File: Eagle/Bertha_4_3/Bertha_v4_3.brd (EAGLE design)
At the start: 100 x 84.6 mm, 89 parts, among them CON1 JACK_DC_BARREL, IC1 MCP1703DB, J1 RJ12RIGHTANGLE-I2C, J2 RJ12RIGHTANGLE-I2C, Q5 BSP75, Q6 BSP75, U1 HX711, X2 16MHz, X3 FH12-08S-1SH, X4 MINI-USB

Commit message: new v4.3, removed bistable control of the stepper, now on pins A0/A1/D8/D9, control sequence must be adapted in the arduino code. Started to work on the ph_V5.0 board, need to add two steppers and the analog backend circuit
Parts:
- removed 5V1: (no value), Headerlibrary:1X01
- removed C16, C17: 100nF, rcl:C1206
- removed CU5, CU6: 10uF, rcl:C1206
- removed D3, D5: 1N581D1206, lpatiny:LED-1206
- removed LDPW5: RED, adafruit:CHIP-LED0805
- removed R13: 1k, resistor:R0805
- removed R8: 1K, rcl:R0805
- removed U$2: NCP1117LPST50T3G, lpatiny:SOT223
- removed U$6: TXB0104, lpatiny:SO14
- added 100K: 100k, rcl:R0805
- added AN_OUT, LORA_RST: (no value), Headerlibrary:1X01
- added C3, C4: 100nF, rcl:C1206
- added HX1: IRF3704S, transistor-power:D2PACK
- added J7: 22--02, lpatiny:2-PIN-5.08S
- added JP2: (no value), SparkFun-Connectors:1X02
- added LDM1, LDM2, LDM3, LDM4, LDPID, RXLD, TXLD: RED, adafruit:CHIP-LED0805
- added Q1, Q2, Q3, Q4: BSP75, infineon:PG-SOT-223
- added R10, R11, R9: 1K, rcl:R0805
- added RK10, RK11, RK8, RK9: 10K, rcl:R0805
- added RK14, RK15, RK16: 10k, rcl:R0805
- added RT1, RT2: 4.7k, resistor:R1206
- added SJ4, SJ5, SJ6: (no value), SparkFun-Passives:PAD-JUMPER-2-NC_BY_TRACE_YES_SILK
- added STEPPER: (no value), con-lsta:FE06
- added U$4: DS18B20, lpatiny:SO8
- added U$8: DS18B20_SMALLPADS, lpatiny:SMALLPADS_X3
- added U100: RN2483, Octanis1:RN2483
- X2: value 16MHz -> 8MHz
- moved C2 19.0 mm to (35.8, 19.1)
- moved CU4 18.9 mm to (35.8, 16.3)
- moved R12 16.0 mm to (10.7, 23.3), turned to 180 degrees
- moved LDPW12 9.76 mm to (15.2, 23.3), turned to 270 degrees
- moved RK19 7.58 mm to (19.3, 39.3)
- moved LDMEM 6.66 mm to (23.3, 39.3), turned to 270 degrees
- moved LDPW3 4.34 mm to (15.2, 25.8)
- moved R14 4.25 mm to (10.6, 25.8)
- moved IN 1.60 mm to (63.7, 38.8)
- moved CU8 0.59 mm to (5.89, 2.12)
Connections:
- removed net +5V: CU5.1, D3.A, U$2.2, U$2.4
- removed net +5V/1: 32U4.14, 32U4.2, 32U4.24, 32U4.34, 32U4.44, 5V1.1, BJ1.2, C1.1, C12.2, C17.2, C2.1, C6.1, CU1.1, CU3.1, CU4.1, CU7.1, D2.C, D3.C, D4.C, IC1.1, J1.+5V, J2.+5V, R13.1, R8.2, RK1.1, RK18.1, RK19.1, RK2.1, RK5.2, RK6.2, U$6.14, U1.1, U1.16, X3.1, X3.2
- removed net FMOSI: D5.A, RK4.1, U$1.SI
- removed net MISO3: U$1.SO, U$6.4
- removed net MOSI3: D5.C, U$6.3
- removed net N$12: LDPW5.A, R13.2
- removed net N$4: R8.1, U$6.8
- removed net SCK3: RK3.1, U$6.5
- removed net SC_MEM: R3.2, U$6.6
- new net 5: J1.+5V, J2.+5V
- new net ANGND: C3.2, C4.2, SJ4.2, SJ5.2, SJ6.2, U100.P$1, U100.P$11, U100.P$20, U100.P$21, U100.P$22, U100.P$24, U100.P$26, U100.P$27, U100.P$28, U100.P$33, U100.P$41, U100.P$47, U100.P$8
- new net ANT868: AN_OUT.1, U100.P$23
- new net B+: JP2.1, U1.10
- new net B-: JP2.2, U1.9
- new net N$14: Q4.2, RK8.1, STEPPER.1
- new net N$15: Q2.2, RK9.1, STEPPER.3
- new net N$16: Q3.2, RK10.1, STEPPER.4
- new net N$18: RK15.2, TXLD.A
- new net N$19: Q1.2, RK11.1, STEPPER.6
- new net N$21: R9.2, RT1.2, U$8.PIN2
- new net N$24: RK16.2, RXLD.A
- new net N$26: LDPID.A, RK14.1
- new net N$31: LDM4.C, RK8.2
- new net N$32: LDM3.C, RK9.2
- new net N$33: LDM2.C, RK10.2
- new net N$36: HX1.2, J7.2
- new net N$37: LDM1.C, RK11.2
- new net N$6: HX1.1, R11.2, RK14.2
- new net N$9: R10.2, RT2.2, U$4.4
- net +12V: now also C1.1, C2.1, CU3.1, CU4.1, CU7.1, D2.C, D4.C, IC1.1, J7.1, LDM1.A, LDM2.A, LDM3.A, LDM4.A, STEPPER.2, STEPPER.5, X3.1, X3.2; no longer CU6.1, U$2.3
- net 3.3V: now also 100K.1, 32U4.14, 32U4.2, 32U4.24, 32U4.34, 32U4.44, BJ1.2, C12.2, C3.1, C4.1, C6.1, CU1.1, RK1.1, RK15.1, RK16.1, RK18.1, RK19.1, RK2.1, RK5.2, RK6.2, RT1.1, RT2.1, U$4.3, U$8.PIN3, U1.1, U1.16, U100.P$12, U100.P$34; no longer C16.2, U$6.1
- net A0: now also Q3.1
- net A1: now also Q1.1
- net A6: now also R9.1
- net D10*: now also R3.2; no longer U$6.9
- net D12*: now also R11.1
- net D5*: now also 100K.2, LORA_RST.1, U100.P$32
- net D6*: now also R10.1
- net D8*: now also Q4.1
- net D9*: now also Q2.1
- net GND: now also HX1.3, LDPID.C, Q1.3, Q2.3, Q3.3, Q4.3, SJ4.1, SJ5.1, SJ6.1, U$4.5, U$8.PIN1; no longer C16.1, C17.1, CU5.2, CU6.2, LDPW5.C, U$2.1, U$6.7
- net MISO: now also U$1.SO; no longer U$6.11
- net MOSI: now also RK4.1, U$1.SI; no longer U$6.12
- net RX: now also U100.P$6
- net RXLED: now also RXLD.C
- net SCK: now also RK3.1; no longer U$6.10
- net TX: now also U100.P$7
- net TXLED: now also TXLD.C
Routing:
- net +5V/1: track 451.3 -> 0.00 mm, vias 7 -> 0
- net 3.3V: track 182.3 -> 480.4 mm, vias 4 -> 18
- net +12V: track 133.3 -> 334.4 mm, vias 0 -> 2
- net D5*: track 0.00 -> 164.8 mm, vias 0 -> 3
- net RX: track 0.00 -> 102.2 mm, vias 0 -> 5
- net TX: track 0.00 -> 97.3 mm, vias 0 -> 5
- net D12*: track 0.00 -> 63.0 mm, vias 0 -> 2
- net D10*: track 0.00 -> 57.9 mm, vias 0 -> 2
- net A1: track 0.00 -> 48.2 mm, vias 0 -> 2
- net GND: track 124.0 -> 171.7 mm, vias 29 -> 39
- net D8*: track 0.00 -> 39.2 mm, vias 0 -> 2
- net N$14: track 0.00 -> 36.3 mm
- net D9*: track 0.00 -> 35.1 mm, vias 0 -> 2
- net MISO: track 76.9 -> 112.0 mm
- net MOSI: track 85.0 -> 119.9 mm, vias 2 -> 4
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- added copper zone on layer 16, net ANGND
- added copper zone on layer 1, net GND
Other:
- board text added: "BerthaV4.3"
- board text added: "D8"
- board text added: "D9"
- board text added: "MEM SELECT"
- board text removed: "BerthaV4.1"
- board text removed: "MEM"
- board text removed: "No LoRa"

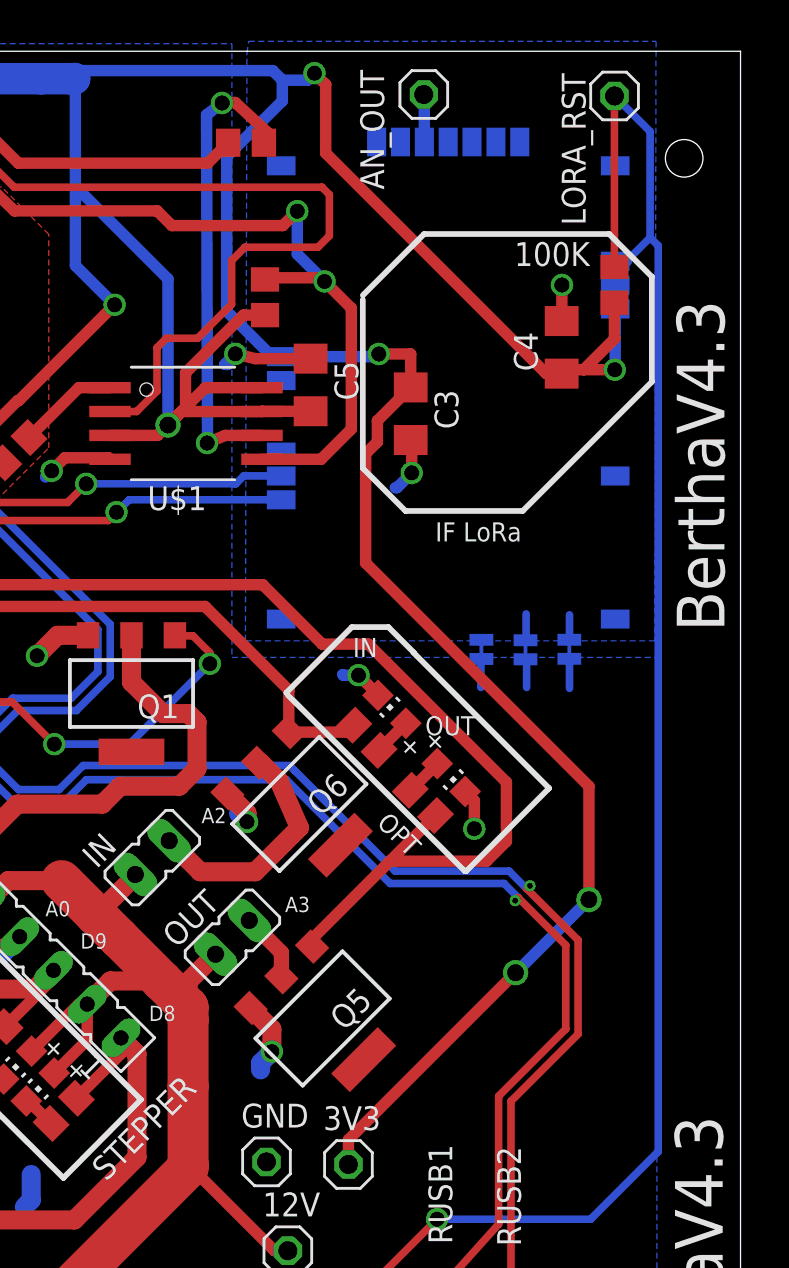
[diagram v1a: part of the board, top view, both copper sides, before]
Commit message: Added SMA LoRa antenna for 4.3 ref #18, same needs to be done for the pH board
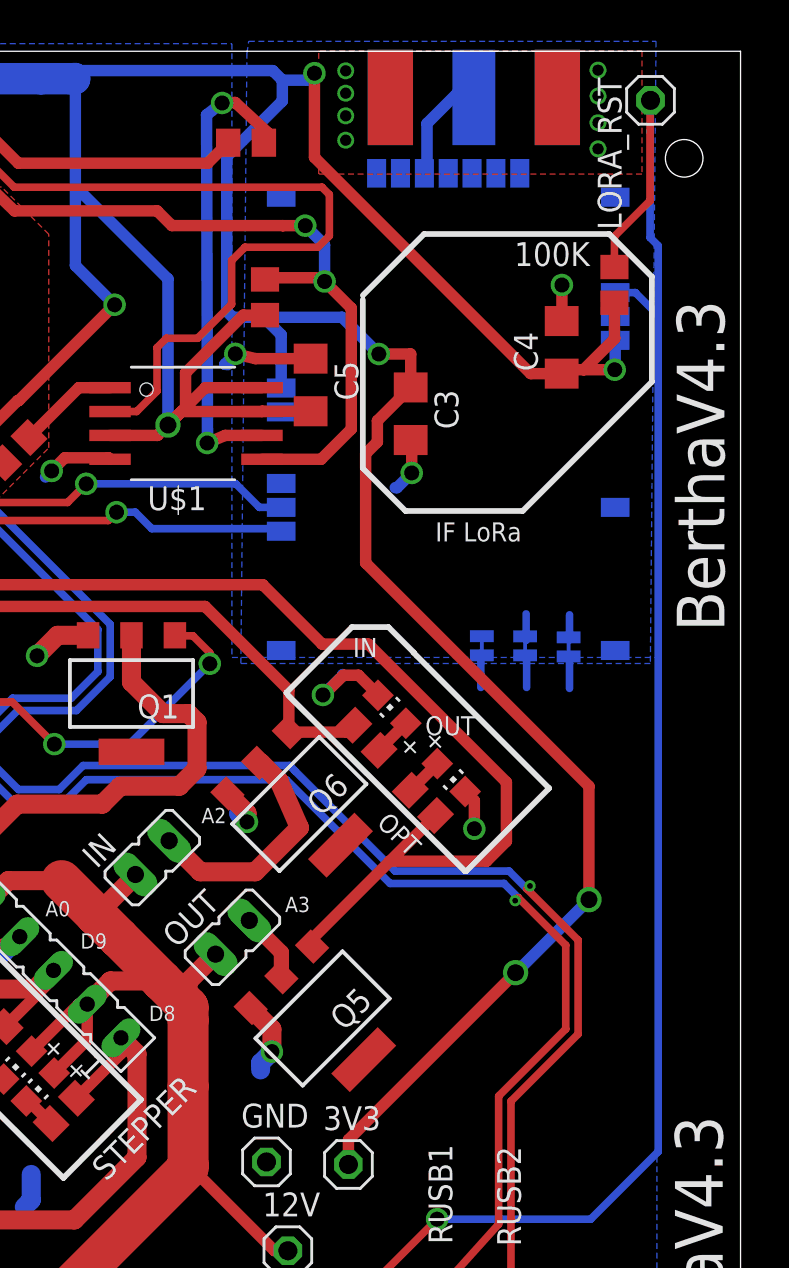
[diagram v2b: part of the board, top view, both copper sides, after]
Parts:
- removed AN_OUT: (no value), Headerlibrary:1X01
- added 868MHZ: (no value), sma_end_launch:SMA_EDGELAUNCH
- moved LORA_RST 1.93 mm to (90.2, 79.1)
- moved U100 1.67 mm to (88.3, 48.5)
- moved SJ4 0.21 mm to (83.5, 50.0)
- moved SJ5 0.20 mm to (81.2, 50.1)
- moved SJ6 0.13 mm to (85.8, 50.0)
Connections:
- net ANGND: now also 868MHZ.GND@1, 868MHZ.GND@2, 868MHZ.GND@3, 868MHZ.GND@4
- net ANT868: now also 868MHZ.P; no longer AN_OUT.1
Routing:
- net GND: track 171.7 -> 175.2 mm
- net 3.3V: track 480.4 -> 483.8 mm
- net ANT868: track 2.54 -> 5.91 mm
- net MOSI: track 119.9 -> 119.1 mm
- net ANGND: track 7.79 -> 8.09 mm, vias 2 -> 10
- added copper zone on layer 1, net ANGND
